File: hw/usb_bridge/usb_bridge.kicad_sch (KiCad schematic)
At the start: 43 parts, among them J1 USB_C_Receptacle_USB2.0_14P, J2 DE9, U1 CH340E, U2 MAX485E, U3 CH334R, U4 74LVC2G04, U5 MCP1754S-3302xCB, U6 TJA1051T-3, Y1 HCI XC53G2-12.000-F20LJDT

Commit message: Add license
Signed-off-by: Mateusz Pająk <22417805+Tai-Min@users.noreply.github.com>
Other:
- note added: "This documentation describes Open Hardware and is licensed under the CERN OHL v. 1.2. You may redistribute and modify this documentation under the terms of the CERN OHL v.1.2.(http://ohwr.org/cernohl). This documentation is distributed WITHOUT ANY EXPRESS OR IMPLIED WARRANTY, INCLUDING OF MERCHANTABILITY, SATISFACTORY QUALITY AND FITNESS FOR A PARTICULAR PURPOSE. Please see the CERN OHL v.1.2 for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"
- title: (none) -> USB <-> CAN/RS485 Bridge
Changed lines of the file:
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@@
 	(generator_version "9.0")
 	(paper "A4")
+	(title_block
+		(title "USB <-> CAN/RS485 Bridge")
+		(date "2025-11-24")
+		(rev "1.0")
+	)
 	(rectangle
 		(start 29.21 13.97)
@@
 		)
 	)
+	(text "This documentation describes Open Hardware and is licensed under the CERN OHL v. 1.2.\nYou may redistribute and modify this documentation under the terms of the \nCERN OHL v.1.2.(http://ohwr.org/cernohl). This documentation is distributed \nWITHOUT ANY EXPRESS OR IMPLIED WARRANTY, INCLUDING OF MERCHANTABILITY,\nSATISFACTORY QUALITY AND FITNESS FOR A PARTICULAR PURPOSE.\nPlease see the CERN OHL v.1.2 for applicable conditions"
+		(exclude_from_sim no)
+		(at 231.394 173.99 0)
+		(effects
+			(font
+				(size 1.27 1.27)
+			)
+		)
+	)
 	(text "male"
 		(exclude_from_sim no)
@@
 		)
 		(instances
-			(project "bridge"
+			(project "usb_bridge"
 				(path "/3b0cc3d4-df75-4145-abb6-d19d57c31f1b"
 					(page "2")

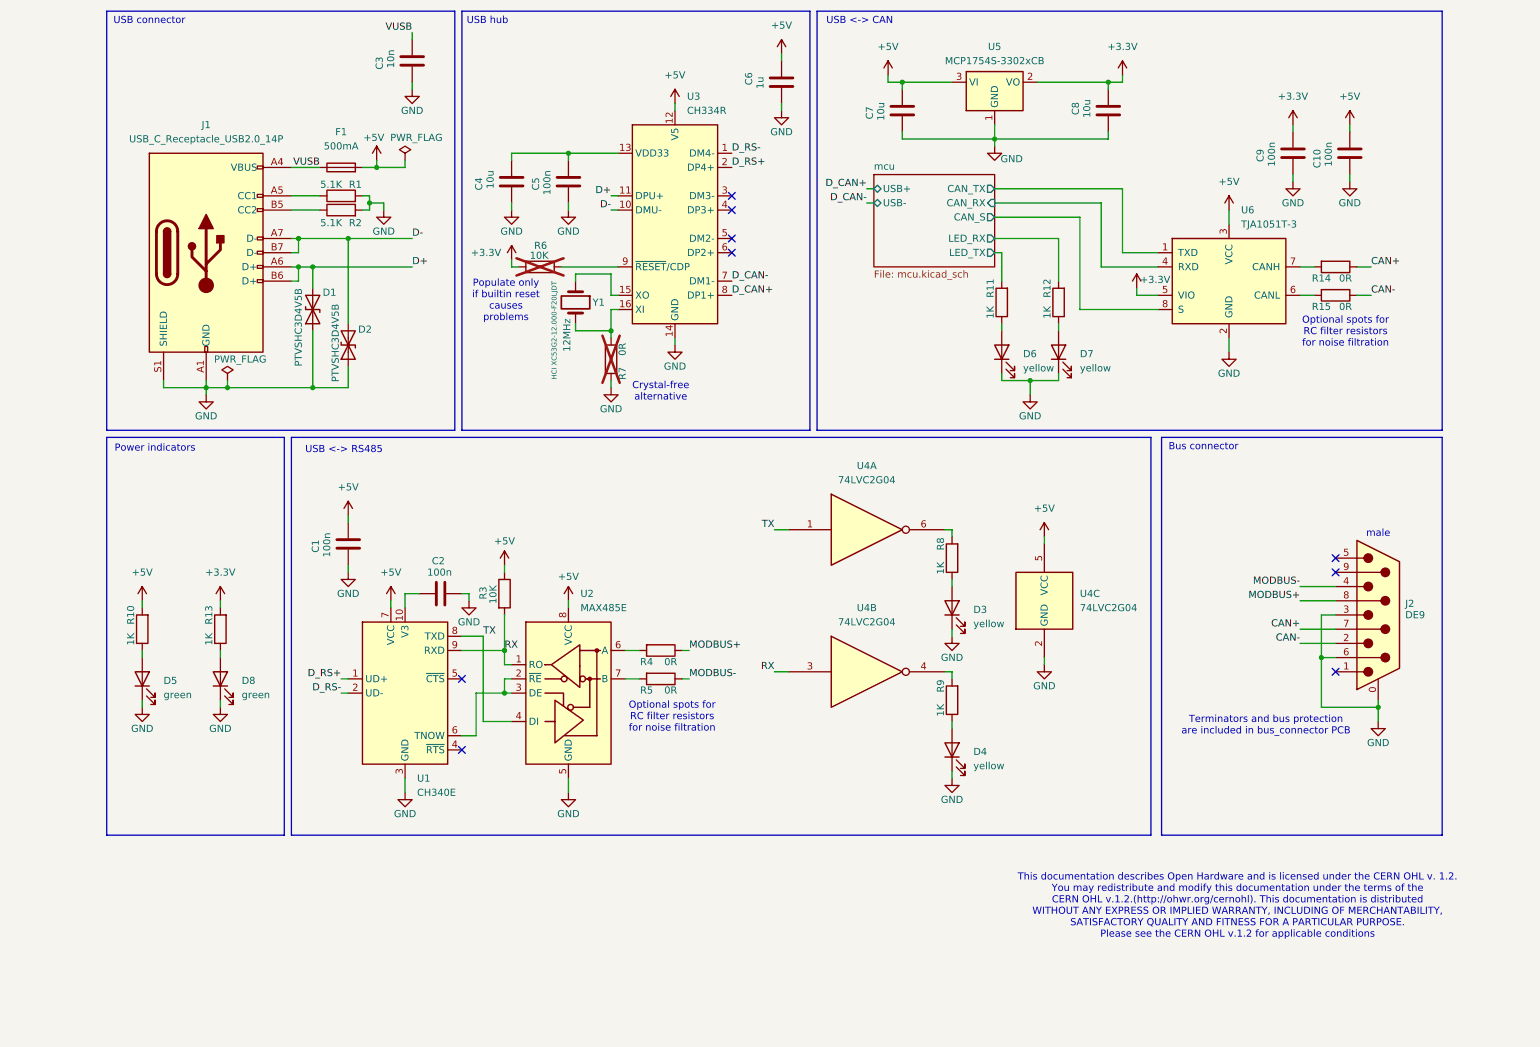
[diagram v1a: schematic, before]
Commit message: Add jumpers and test points, add QR code
Signed-off-by: Mateusz Pająk <22417805+Tai-Min@users.noreply.github.com>
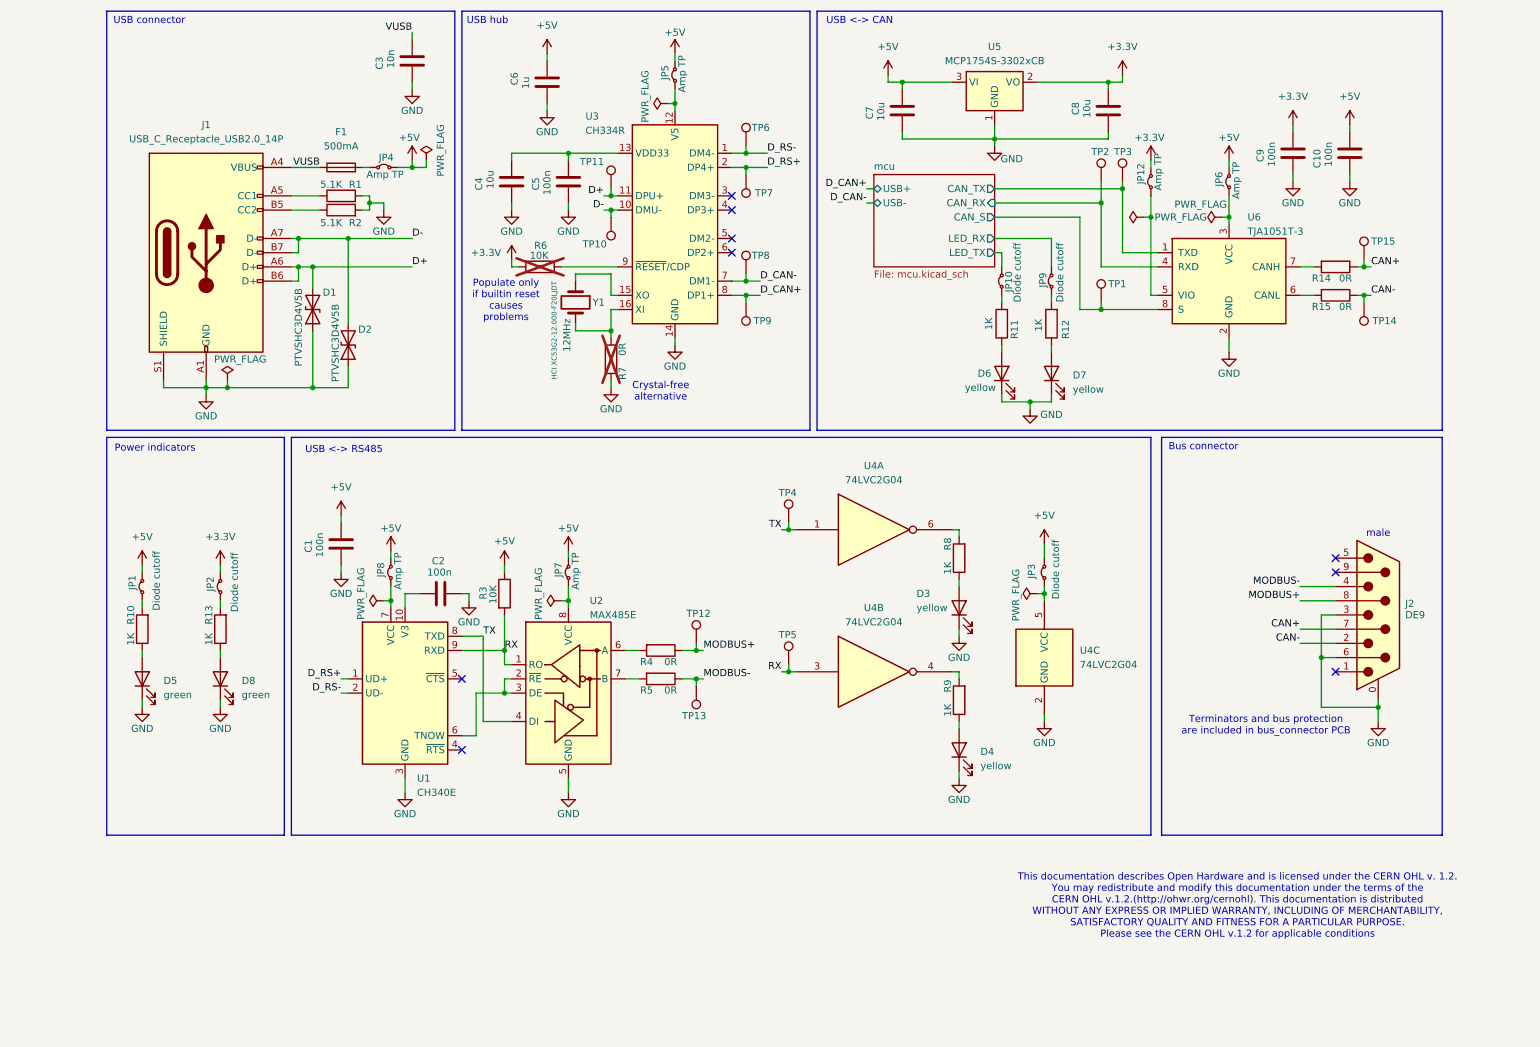
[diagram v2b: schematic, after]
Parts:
- added JP1, JP10, JP2, JP3, JP9: Diode cutoff, Jumper:SolderJumper-2_P1.3mm_Bridged_Pad1.0x1.5mm, symbol Jumper:Jumper_2_Small_Bridged
- added JP12, JP4, JP5, JP6, JP7, JP8: Amp TP, Jumper:SolderJumper-2_P1.3mm_Bridged_Pad1.0x1.5mm, symbol Jumper:Jumper_2_Small_Bridged
- added TP1, TP10, TP11, TP12, TP13, TP14, TP15, TP2, TP3, TP4, TP5, TP6, TP7, TP8, TP9: TestPoint, TestPoint:TestPoint_Pad_D1.5mm, symbol Connector:TestPoint
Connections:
- net +3.3V: now also JP12.2 (B), JP2.2 (B); no longer R13.2, U6.5 (VIO)
- net +5V: now also JP1.2 (B), JP3.2 (B), JP4.2 (B), JP5.2 (B), JP6.2 (B), JP7.2 (B), JP8.2 (B); no longer F1.2, R10.2, U1.7 (VCC), U2.8 (VCC), U3.12 (V5), U4.5 (VCC), U6.3 (VCC)
- net CAN+: now also TP15.1
- net CAN-: now also TP14.1
- net D+: now also TP11.1
- net D-: now also TP10.1
- net D_CAN+: now also TP9.1
- net D_CAN-: now also TP8.1
- net D_RS+: now also TP7.1
- net D_RS-: now also TP6.1
- net MODBUS+: now also TP12.1
- net MODBUS-: now also TP13.1
- net RX: now also TP5.1
- net TX: now also TP4.1
- net mcu/CAN_RX: now also TP2.1
- net mcu/CAN_S: now also TP1.1
- net mcu/CAN_TX: now also TP3.1
- net mcu/LED_RX: now also JP9.2 (B); no longer R12.2
- net mcu/LED_TX: now also JP10.2 (B); no longer R11.2
- new net: JP9.1 (A), R12.2
- new net: JP8.1 (A), U1.7 (VCC)
- new net: JP2.1 (A), R13.2
- new net: JP5.1 (A), U3.12 (V5)
- new net: JP10.1 (A), R11.2
- new net: JP3.1 (A), U4.5 (VCC)
- new net: F1.2, JP4.1 (A)
- new net: JP12.1 (A), U6.5 (VIO)
- new net: JP6.1 (A), U6.3 (VCC)
- new net: JP7.1 (A), U2.8 (VCC)
- new net: JP1.1 (A), R10.2
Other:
- note removed: "Optional spots for RC filter resistors for noise filtration"
- moved on the sheet: C1, C6, D3, D4, D6, D7, R11, R12, R8, R9, U4A, U4B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

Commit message: Add gnd test point
Signed-off-by: Mateusz Pająk <22417805+Tai-Min@users.noreply.github.com>
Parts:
- added TP16: TestPoint, TestPoint:TestPoint_Pad_D1.5mm, symbol Connector:TestPoint
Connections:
- net GND: now also TP16.1
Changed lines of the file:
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@@
 	(wire
 		(pts
+			(xy 86.36 80.01) (xy 86.36 81.28)
+		)
+		(stroke
+			(width 0)
+			(type default)
+		)
+	)
+	(wire
+		(pts
 			(xy 66.04 71.12) (xy 66.04 81.28)
 		)
@@
 	)
 	(symbol
+		(lib_id "Connector:TestPoint")
+		(at 86.36 80.01 0)
+		(unit 1)
+		(exclude_from_sim no)
+		(in_bom yes)
+		(on_board yes)
+		(dnp no)
+		(property "Reference" "TP16"
+			(at 80.518 76.708 0)
+			(effects
+				(font
+					(size 1.27 1.27)
+				)
+				(justify left)
+			)
+		)
+		(property "Value" "TestPoint"
+			(at 88.9 77.9779 0)
+			(effects
+				(font
+					(size 1.27 1.27)
+				)
+				(justify left)
+				(hide yes)
+			)
+		)
+		(property "Footprint" "TestPoint:TestPoint_Pad_D1.5mm"
+			(at 91.44 80.01 0)
+			(effects
+				(font
+					(size 1.27 1.27)
+				)
+				(hide yes)
+			)
+		)
+		(property "Datasheet" "~"
+			(at 91.44 80.01 0)
+			(effects
+				(font
+					(size 1.27 1.27)
+				)
+				(hide yes)
+			)
+		)
+		(property "Description" "test point"
+			(at 86.36 80.01 0)
+			(effects
+				(font
+					(size 1.27 1.27)
+				)
+				(hide yes)
+			)
+		)
+		(pin "1"
+		)
+		(instances
+			(project "usb_bridge"
+				(path "/3b0cc3d4-df75-4145-abb6-d19d57c31f1b"
+					(reference "TP16")
+					(unit 1)
+				)
+			)
+		)
+	)
+	(symbol
 		(lib_id "power:GND")
 		(at 256.54 140.97 0)
@@
 					(unit 1)
 				)
+			)
+		)
+	)
+	(symbol
+		(lib_id "power:GND")
+		(at 86.36 81.28 0)
+		(unit 1)
+		(exclude_from_sim no)
+		(in_bom yes)
+		(on_board yes)
+		(dnp no)
+		(property "Reference" "#PWR047"
+			(at 86.36 87.63 0)
+			(effects
+				(font
+					(size 1.27 1.27)
+				)
+				(hide yes)
+			)
+		)
+		(property "Value" "GND"
+			(at 86.36 85.09 0)
+			(effects
+				(font
+					(size 1.27 1.27)
+				)
+			)
+		)
+		(property "Footprint" ""
+			(at 86.36 81.28 0)
+			(effects
+				(font
+					(size 1.27 1.27)
+				)
+				(hide yes)
+			)
+		)
+		(property "Datasheet" ""
+			(at 86.36 81.28 0)
+			(effects
+				(font
+					(size 1.27 1.27)
+				)
+				(hide yes)
+			)
+		)
+		(property "Description" "Power symbol creates a global label with name \"GND\" , ground"
+			(at 86.36 81.28 0)
+			(effects
+				(font
+					(size 1.27 1.27)
+				)
+				(hide yes)
+			)
+		)
+		(pin "1"
+		)
+		(instances
+			(project "usb_bridge"
+				(path "/3b0cc3d4-df75-4145-abb6-d19d57c31f1b"
+					(reference "#PWR047")
+					(unit 1)
+				)

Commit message: Update LCSC BOM
Signed-off-by: Mateusz Pająk <22417805+Tai-Min@users.noreply.github.com>
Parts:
- C1, C10, C2, C5, C9: LCSC https://www.lcsc.com/product-detail/C66501.html -> (none); LCSC Link (none) -> https://www.lcsc.com/product-detail/C66501.html; LCSC Part # (none) -> C66501
- C3: LCSC https://www.lcsc.com/product-detail/C100042.html -> (none); LCSC Link (none) -> https://www.lcsc.com/product-detail/C100042.html; LCSC Part # (none) -> C100042
- C4, C7, C8: LCSC https://www.lcsc.com/product-detail/C92487.html -> (none); LCSC Link (none) -> https://www.lcsc.com/product-detail/C92487.html; LCSC Part # (none) -> C92487
- C6: LCSC https://www.lcsc.com/product-detail/C1592.html -> (none); LCSC Link (none) -> https://www.lcsc.com/product-detail/C1592.html; LCSC Part # (none) -> C1592
- D1, D2: LCSC https://www.lcsc.com/product-detail/C110752.html?s_z=n_PTVS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 -> (none); LCSC Link (none) -> https://www.lcsc.com/product-detail/C110752.html?s_z=n_PTVS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; LCSC Part # (none) -> C110752
- D3, D4, D6, D7: LCSC https://www.lcsc.com/product-detail/C72038.html -> (none); LCSC Link (none) -> https://www.lcsc.com/product-detail/C72038.html; LCSC Part # (none) -> C72038
- D5, D8: LCSC https://www.lcsc.com/product-detail/C22371297.html -> (none); LCSC Link (none) -> https://www.lcsc.com/product-detail/C22371297.html; LCSC Part # (none) -> C22371297
- F1: LCSC https://www.lcsc.com/product-detail/C41380225.html -> (none); LCSC Link (none) -> https://www.lcsc.com/product-detail/C41380225.html; LCSC Part # (none) -> C41380225
- J1: LCSC https://www.lcsc.com/product-detail/C7095263.html?s_z=n_USB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 -> (none); LCSC Link (none) -> https://www.lcsc.com/product-detail/C7095263.html?s_z=n_USB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; LCSC Part # (none) -> C7095263
- J2: LCSC https://www.lcsc.com/product-detail/C19077344.html?s_z=n_ds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 -> (none); LCSC Link (none) -> https://www.lcsc.com/product-detail/C19077344.html?s_z=n_ds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; LCSC Part # (none) -> C19077344
- R1, R2: LCSC https://www.lcsc.com/product-detail/C2907044.html -> (none); LCSC Link (none) -> https://www.lcsc.com/product-detail/C2907044.html; LCSC Part # (none) -> C2907044
- R10, R11, R12, R13, R8, R9: LCSC https://www.lcsc.com/product-detail/C22548.html -> (none); LCSC Link (none) -> https://www.lcsc.com/product-detail/C22548.html; LCSC Part # (none) -> C22548
- R14, R15, R4, R5, R7: LCSC https://www.lcsc.com/product-detail/C95177.html -> (none); LCSC Link (none) -> https://www.lcsc.com/product-detail/C95177.html; LCSC Part # (none) -> C95177
- R3, R6: LCSC https://www.lcsc.com/product-detail/C98220.html -> (none); LCSC Link (none) -> https://www.lcsc.com/product-detail/C98220.html; LCSC Part # (none) -> C98220
- U1: LCSC https://www.lcsc.com/product-detail/C99652.html?s_z=n_ch340e -> (none); LCSC Link (none) -> https://www.lcsc.com/product-detail/C99652.html?s_z=n_ch340e; LCSC Part # (none) -> C99652
- U2: LCSC https://www.lcsc.com/product-detail/C481667.html?s_z=n_max4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 -> (none); LCSC Link (none) -> https://www.lcsc.com/product-detail/C481667.html?s_z=n_max4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; LCSC Part # (none) -> C481667
- U3: LCSC https://www.lcsc.com/product-detail/C4154405.html?s_z=n_ch3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 -> (none); LCSC Link (none) -> https://www.lcsc.com/product-detail/C4154405.html?s_z=n_ch3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; LCSC Part # (none) -> C4154405
- U4: LCSC https://www.lcsc.com/product-detail/C19829596.html?s_z=n_74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 -> (none); LCSC Link (none) -> https://www.lcsc.com/product-detail/C19829596.html?s_z=n_74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; LCSC Part # (none) -> C19829596
- U5: LCSC https://www.lcsc.com/product-detail/C625392.html?s_z=n_MCP1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 -> (none); LCSC Link (none) -> https://www.lcsc.com/product-detail/C625392.html?s_z=n_MCP1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; LCSC Part # (none) -> C625392
- U6: LCSC https://www.lcsc.com/product-detail/C51954344.html?s_z=n_TJ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 -> (none); LCSC Link (none) -> https://www.lcsc.com/product-detail/C51954344.html?s_z=n_TJ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; LCSC Part # (none) -> C51954344
- Y1: LCSC https://www.lcsc.com/product-detail/C2842275.html?s_z=n_HCI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 -> (none); LCSC Link (none) -> https://www.lcsc.com/product-detail/C2842275.html?s_z=n_HCI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; LCSC Part # (none) -> C2842275

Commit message: Update datasheets
Signed-off-by: Mateusz Pająk <22417805+Tai-Min@users.noreply.github.com>
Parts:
- C1, C10, C2, C5, C9: LCSC Link https://www.lcsc.com/product-detail/C66501.html -> (none)
- C3: LCSC Link https://www.lcsc.com/product-detail/C100042.html -> (none)
- C4, C7, C8: LCSC Link https://www.lcsc.com/product-detail/C92487.html -> (none)
- C6: LCSC Link https://www.lcsc.com/product-detail/C1592.html -> (none)
- D1, D2: LCSC Link https://www.lcsc.com/product-detail/C110752.html?s_z=n_PTVS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 -> (none)
- D3, D4, D6, D7: LCSC Link https://www.lcsc.com/product-detail/C72038.html -> (none)
- D5, D8: LCSC Link https://www.lcsc.com/product-detail/C22371297.html -> (none)
- F1: LCSC Link https://www.lcsc.com/product-detail/C41380225.html -> (none)
- J1: LCSC Link https://www.lcsc.com/product-detail/C7095263.html?s_z=n_USB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 -> (none)
- J2: LCSC Link https://www.lcsc.com/product-detail/C19077344.html?s_z=n_ds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 -> (none)
- R1, R2: LCSC Link https://www.lcsc.com/product-detail/C2907044.html -> (none)
- R10, R11, R12, R13, R8, R9: LCSC Link https://www.lcsc.com/product-detail/C22548.html -> (none)
- R14, R15, R4, R5, R7: LCSC Link https://www.lcsc.com/product-detail/C95177.html -> (none)
- R3, R6: LCSC Link https://www.lcsc.com/product-detail/C98220.html -> (none)
- U1: LCSC Link https://www.lcsc.com/product-detail/C99652.html?s_z=n_ch340e -> (none)
- U2: LCSC Link https://www.lcsc.com/product-detail/C481667.html?s_z=n_max4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 -> (none)
- U3: LCSC Link https://www.lcsc.com/product-detail/C4154405.html?s_z=n_ch3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 -> (none)
- U4: LCSC Link https://www.lcsc.com/product-detail/C19829596.html?s_z=n_74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 -> (none)
- U5: LCSC Link https://www.lcsc.com/product-detail/C625392.html?s_z=n_MCP1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 -> (none)
- U6: LCSC Link https://www.lcsc.com/product-detail/C51954344.html?s_z=n_TJ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 -> (none)
- Y1: Freq 12MHz -> (none); LCSC Link https://www.lcsc.com/product-detail/C2842275.html?s_z=n_HCI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 -> (none)

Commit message: Cleanup
Signed-off-by: Mateusz Pająk <22417805+Tai-Min@users.noreply.github.com>
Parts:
- removed D8: green, LED_SMD:LED_0603_1608Metric, symbol Device:LED
- removed JP1, JP10, JP2, JP3, JP9: Diode cutoff, Jumper:SolderJumper-2_P1.3mm_Bridged_Pad1.0x1.5mm, symbol Jumper:Jumper_2_Small_Bridged
- removed JP12, JP4, JP5, JP6, JP7, JP8: Amp TP, Jumper:SolderJumper-2_P1.3mm_Bridged_Pad1.0x1.5mm, symbol Jumper:Jumper_2_Small_Bridged
- removed R13: 1K, Resistor_SMD:R_0603_1608Metric, symbol Device:R
- removed TP10, TP11: TestPoint, TestPoint:TestPoint_Pad_D1.5mm, symbol Connector:TestPoint
- added D8: CDSOT23-T24CAN, Package_TO_SOT_SMD:SOT-23, symbol Diode:SM712_SOT23
- added D9: SM712-02HTG, Package_TO_SOT_SMD:SOT-23, symbol Diode:SM712_SOT23
- F1: value 500mA -> BSMD0603C-0500T
- renumbered C3 to C2, C2 to C3, C6 to C5, C5 to C6, D5 to D1, D1 to D2, D2 to D3, D3 to D4, D4 to D5, R10 to R1, R9 to R10, R14 to R13, R15 to R14, R1 to R2, R2 to R3, R3 to R4, R6 to R5, R7 to R6, R4 to R7, R5 to R8, R8 to R9, TP16 to TP1, TP4 to TP10, TP5 to TP11, TP1 to TP12, TP2 to TP13, TP3 to TP14, TP14 to TP16, TP12 to TP4, TP13 to TP5
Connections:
- net +3.3V: now also U6.5 (VIO)
- net +5V: now also F1.2, R1.2, U1.7 (VCC), U2.8 (VCC), U3.12 (V5), U4.5 (VCC), U6.3 (VCC)
- net CAN+: now also D8.2 (A2)
- net CAN-: now also D8.1 (A1)
- net GND: now also D8.3 (common), D9.3 (common)
- net MODBUS+: now also D9.2 (A2)
- net MODBUS-: now also D9.1 (A1)
- net mcu/LED_RX: now also R12.2
- net mcu/LED_TX: now also R11.2
- net RX renamed RS_RX
- net TX renamed RS_TX
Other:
- note added: "Bus protection"
- note removed: "Terminators and bus protection are included in bus_connector PCB"
- note removed: "This documentation describes Open Hardware and is licensed under the CERN OHL v. 1.2. You may redistribute and modify this documentation under the terms of the CERN OHL v.1.2.(http://ohwr.org/cernohl). This documentation is distributed WITHOUT ANY EXPRESS OR IMPLIED WARRANTY, INCLUDING OF MERCHANTABILITY, SATISFACTORY QUALITY AND FITNESS FOR A PARTICULAR PURPOSE. Please see the CERN OHL v.1.2 for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"
- moved on the sheet: C1, C2, C3, D1, D4, D5, D6, D7, R1, R10, R11, R12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
